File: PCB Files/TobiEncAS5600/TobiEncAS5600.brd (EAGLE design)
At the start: 10 x 16 mm, 4 parts

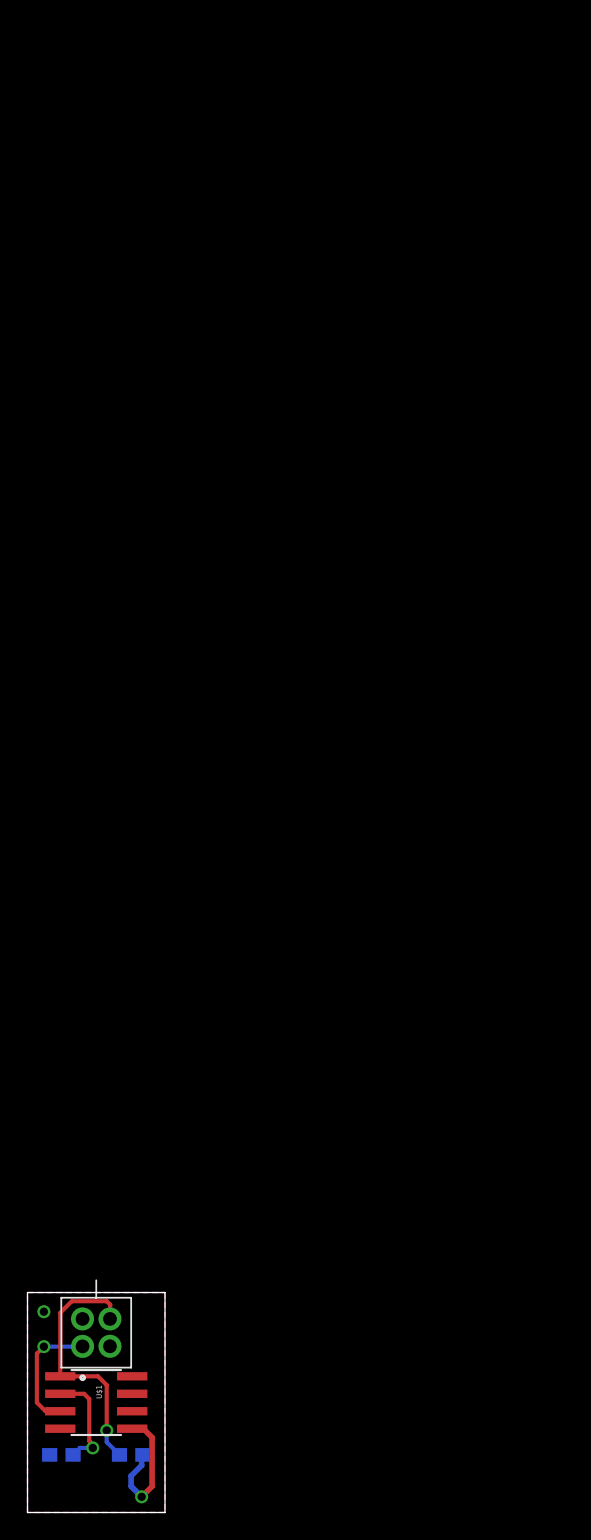
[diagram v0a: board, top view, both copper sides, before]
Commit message: position components for wider encoder board
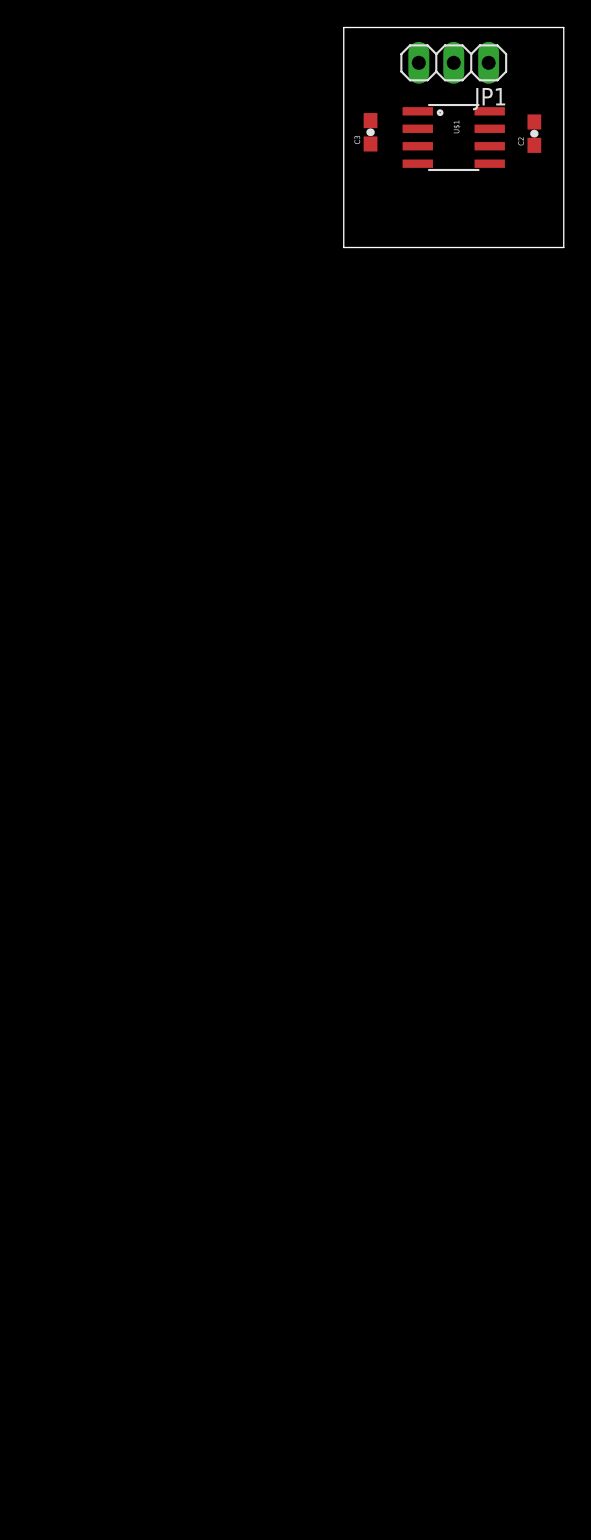
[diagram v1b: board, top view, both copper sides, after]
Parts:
- removed U$2: DF11-4PIN, Gavin:DF11-4PIN
- added JP1: (no value), pinhead:1X03
- moved C2 100.5 mm to (31.9, 92.3), flipped to the top, turned to 90 degrees
- moved C3 98.8 mm to (19.9, 92.4), flipped to the top, turned to 90 degrees
- moved U$1 95.6 mm to (26.0, 92.0)
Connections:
- net N$1 renamed VDD3V3
- net 5V: now also JP1.1; no longer U$2.P2
- net GND: now also JP1.2; no longer U$2.P1
- net SIG: now also JP1.3; no longer U$2.P3
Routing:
- net 5V: track 18.9 -> 0.00 mm, vias 1 -> 0
- net GND: track 10.1 -> 0.00 mm, vias 2 -> 0
- net SIG: track 9.06 -> 0.00 mm, vias 1 -> 0
- net VDD3V3: track 7.57 -> 0.00 mm, vias 1 -> 0
- removed copper zone on layer 1, net GND
- removed copper zone on layer 16, net GND
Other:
- board size 10 x 16 mm -> 16 x 16 mm
- board text removed: "5V"
- board text removed: "GND"
- board text removed: "SIG"

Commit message: double wide encoder board
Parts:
- moved C2 11.4 mm to (20.5, 92.7)
- moved C3 3.54 mm to (20.4, 88.9)
- moved JP1 0.68 mm to (26.0, 96.8)
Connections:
- net GND: now also U$1.6, U$1.7
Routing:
- net GND: track 0.00 -> 21.3 mm
- net 5V: track 0.00 -> 14.7 mm
- net SIG: track 0.00 -> 6.83 mm
- net VDD3V3: track 0.00 -> 4.51 mm
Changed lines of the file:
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@@
 <param name="RoutingGrid" value="50mil"/>
 <param name="AutoGrid" value="1"/>
-<param name="Efforts" value="0"/>
+<param name="Efforts" value="2"/>
 <param name="TopRouterVariant" value="1"/>
 <param name="tpViaShape" value="round"/>
@@
 </autorouter>
 <elements>
-<element name="C2" library="SparkFun-Capacitors" package="0603-CAP" value="100nf" x="31.86" y="92.28" rot="R90"/>
-<element name="C3" library="SparkFun-Capacitors" package="0603-CAP" value="1uf" x="19.95" y="92.38" rot="R90"/>
-<element name="JP1" library="pinhead" library_urn="urn:adsk.eagle:library:325" package="1X03" value="" x="26" y="97.43" rot="R180"/>
+<element name="C2" library="SparkFun-Capacitors" package="0603-CAP" value="100nf" x="20.46" y="92.68" rot="R90"/>
+<element name="C3" library="SparkFun-Capacitors" package="0603-CAP" value="1uf" x="20.45" y="88.88" rot="R90"/>
+<element name="JP1" library="pinhead" library_urn="urn:adsk.eagle:library:325" package="1X03" value="" x="26" y="96.75" rot="R180"/>
 <element name="U$1" library="Gavin" package="SO08" value="AS5600" x="26" y="92" rot="R270"/>
 </elements>
@@
 <contactref element="C2" pad="2"/>
 <contactref element="JP1" pad="1"/>
-<wire x1="28.54" y1="97.43" x2="23.3838" y2="93.905" width="0" layer="19" extent="1-1"/>
-<wire x1="31.86" y1="93.13" x2="28.54" y2="97.43" width="0" layer="19" extent="1-1"/>
+<wire x1="23.0124" y1="93.5736" x2="22.2504" y2="93.5736" width="0.1524" layer="1"/>
+<wire x1="22.2504" y1="93.5736" x2="20.574" y2="93.5736" width="0.1524" layer="1"/>
+<wire x1="23.3172" y1="93.8784" x2="23.0124" y2="93.5736" width="0.1524" layer="1"/>
+<wire x1="20.574" y1="93.5736" x2="20.46" y2="93.53" width="0.1524" layer="1"/>
+<wire x1="23.3172" y1="93.8784" x2="23.3838" y2="93.905" width="0.1524" layer="1"/>
+<wire x1="22.2504" y1="97.8408" x2="22.2504" y2="93.5736" width="0.1524" layer="1"/>
+<wire x1="23.0124" y1="98.6028" x2="22.2504" y2="97.8408" width="0.1524" layer="1"/>
+<wire x1="26.67" y1="98.6028" x2="23.0124" y2="98.6028" width="0.1524" layer="1"/>
+<wire x1="28.4988" y1="96.774" x2="26.67" y2="98.6028" width="0.1524" layer="1"/>
+<wire x1="28.4988" y1="96.774" x2="28.54" y2="96.75" width="0.1524" layer="1"/>
 </signal>
 <signal name="SIG">
 <contactref element="U$1" pad="3"/>
 <contactref element="JP1" pad="3"/>
-<wire x1="23.46" y1="97.43" x2="23.3838" y2="91.365" width="0" layer="19" extent="1-1"/>
+<wire x1="23.9268" y1="91.44" x2="23.4696" y2="91.44" width="0.1524" layer="1"/>
+<wire x1="24.8412" y1="92.3544" x2="23.9268" y2="91.44" width="0.1524" layer="1"/>
+<wire x1="24.8412" y1="95.25" x2="24.8412" y2="92.3544" width="0.1524" layer="1"/>
+<wire x1="23.4696" y1="96.6216" x2="24.8412" y2="95.25" width="0.1524" layer="1"/>
+<wire x1="23.4696" y1="91.44" x2="23.3838" y2="91.365" width="0.1524" layer="1"/>
+<wire x1="23.4696" y1="96.6216" x2="23.46" y2="96.75" width="0.1524" layer="1"/>
 </signal>
 <signal name="GND">
@@
 <contactref element="C3" pad="1"/>
 <contactref element="JP1" pad="2"/>
-<wire x1="28.6162" y1="90.095" x2="23.3838" y2="90.095" width="0" layer="19" extent="1-1"/>
-<wire x1="28.6162" y1="93.905" x2="28.6162" y2="90.095" width="0" layer="19" extent="1-1"/>
-<wire x1="26" y1="97.43" x2="28.6162" y2="93.905" width="0" layer="19" extent="1-1"/>
-<wire x1="31.86" y1="91.43" x2="26" y2="97.43" width="0" layer="19" extent="1-1"/>
-<wire x1="19.95" y1="91.53" x2="31.86" y2="91.43" width="0" layer="19" extent="1-1"/>
+<contactref element="U$1" pad="7"/>
+<contactref element="U$1" pad="6"/>
+<wire x1="21.336" y1="88.0872" x2="20.574" y2="88.0872" width="0.1524" layer="1"/>
+<wire x1="23.3172" y1="90.0684" x2="21.336" y2="88.0872" width="0.1524" layer="1"/>
+<wire x1="20.574" y1="88.0872" x2="20.45" y2="88.03" width="0.1524" layer="1"/>
+<wire x1="23.3172" y1="90.0684" x2="23.3838" y2="90.095" width="0.1524" layer="1"/>
+<wire x1="20.4216" y1="91.1352" x2="20.4216" y2="91.7448" width="0.1524" layer="1"/>
+<wire x1="19.6596" y1="90.3732" x2="20.4216" y2="91.1352" width="0.1524" layer="1"/>
+<wire x1="19.6596" y1="88.8492" x2="19.6596" y2="90.3732" width="0.1524" layer="1"/>
+<wire x1="20.4216" y1="88.0872" x2="19.6596" y2="88.8492" width="0.1524" layer="1"/>
+<wire x1="20.4216" y1="91.7448" x2="20.46" y2="91.83" width="0.1524" layer="1"/>
+<wire x1="20.4216" y1="88.0872" x2="20.45" y2="88.03" width="0.1524" layer="1"/>
+<wire x1="28.6512" y1="91.2876" x2="28.6512" y2="90.2208" width="0.1524" layer="1"/>
+<wire x1="28.6512" y1="90.2208" x2="28.6162" y2="90.095" width="0.1524" layer="1"/>
+<wire x1="28.6512" y1="91.2876" x2="28.6162" y2="91.365" width="0.1524" layer="1"/>
+<wire x1="28.6512" y1="91.44" x2="28.6512" y2="92.5068" width="0.1524" layer="1"/>
+<wire x1="28.6512" y1="92.5068" x2="28.6162" y2="92.635" width="0.1524" layer="1"/>
+<wire x1="28.6512" y1="91.44" x2="28.6162" y2="91.365" width="0.1524" layer="1"/>
+<wire x1="28.6512" y1="92.6592" x2="28.6512" y2="93.8784" width="0.1524" layer="1"/>
+<wire x1="28.6512" y1="93.8784" x2="28.6162" y2="93.905" width="0.1524" layer="1"/>
+<wire x1="28.6512" y1="92.6592" x2="28.6162" y2="92.635" width="0.1524" layer="1"/>
+<wire x1="28.6512" y1="94.0308" x2="26.0604" y2="96.6216" width="0.1524" layer="1"/>
+<wire x1="26.0604" y1="96.6216" x2="26" y2="96.75" width="0.1524" layer="1"/>
+<wire x1="28.6512" y1="94.0308" x2="28.6162" y2="93.905" width="0.1524" layer="1"/>
+<wire x1="28.4988" y1="90.0684" x2="23.4696" y2="90.0684" width="0.1524" layer="1"/>
+<wire x1="23.4696" y1="90.0684" x2="23.3838" y2="90.095" width="0.1524" layer="1"/>
+<wire x1="28.4988" y1="90.0684" x2="28.6162" y2="90.095" width="0.1524" layer="1"/>
 </signal>
 <signal name="VDD3V3">
 <contactref element="C3" pad="2"/>
 <contactref element="U$1" pad="2"/>
-<wire x1="19.95" y1="93.23" x2="23.3838" y2="92.635" width="0" layer="19" extent="1-1"/>
+<wire x1="20.574" y1="90.3732" x2="20.574" y2="89.7636" width="0.1524" layer="1"/>
+<wire x1="22.7076" y1="92.5068" x2="20.574" y2="90.3732" width="0.1524" layer="1"/>
+<wire x1="23.3172" y1="92.5068" x2="22.7076" y2="92.5068" width="0.1524" layer="1"/>
+<wire x1="20.574" y1="89.7636" x2="20.45" y2="89.73" width="0.1524" layer="1"/>
+<wire x1="23.3172" y1="92.5068" x2="23.3838" y2="92.635" width="0.1524" layer="1"/>
 </signal>
 </signals>
